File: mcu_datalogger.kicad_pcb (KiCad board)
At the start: 2 copper layers, 0 parts

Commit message: Prepared PCB
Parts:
- added BT1: Battery, Connector_PinHeader_2.54mm:PinHeader_1x01_P2.54mm_Vertical, F.Cu at (215.1, 142.3)
- added C1: 0.1uF, Capacitor_SMD:C_0805_2012Metric, F.Cu at (237.3, 132.0)
- added C2: 22pF, Capacitor_SMD:C_0805_2012Metric, F.Cu at (237.3, 135.1)
- added C3: 22pF, Capacitor_SMD:C_0805_2012Metric, F.Cu at (237.3, 138.1)
- added C4: 0.1uF, Capacitor_SMD:C_0805_2012Metric, F.Cu at (237.3, 141.1)
- added C5: 100nF, Capacitor_SMD:C_0805_2012Metric, F.Cu at (237.3, 144.1)
- added D1: LED, LED_SMD:LED_0805_2012Metric, F.Cu at (241.8, 132.1)
- added D2: LED, LED_SMD:LED_0805_2012Metric, F.Cu at (241.8, 135.1)
- added H1: MountingHole, MountingHole:MountingHole_2.1mm, F.Cu at (215.6, 119.9)
- added H2: MountingHole, MountingHole:MountingHole_2.1mm, F.Cu at (215.6, 125.6)
- added H3: MountingHole, MountingHole:MountingHole_2.1mm, F.Cu at (215.6, 131.4)
- added H4: MountingHole, MountingHole:MountingHole_2.1mm, F.Cu at (215.6, 137.1)
- added J1: Conn_01x04_Pin, Connector_PinHeader_2.54mm:PinHeader_1x04_P2.54mm_Vertical, F.Cu at (253.0, 119.3)
- added J2: Conn_01x04_Pin, Connector_PinHeader_2.54mm:PinHeader_1x04_P2.54mm_Vertical, F.Cu at (257.6, 119.3)
- added J3: Conn_02x03_Odd_Even, Connector_PinHeader_2.54mm:PinHeader_2x03_P2.54mm_Vertical, F.Cu at (253.0, 131.6)
- added J4: Conn_01x09_Pin, Connector_PinHeader_2.54mm:PinHeader_1x09_P2.54mm_Vertical, F.Cu at (248.3, 119.3)
- added R1: 10K, Resistor_SMD:R_0805_2012Metric, F.Cu at (220.7, 118.5)
- added R2: 10K, Resistor_SMD:R_0805_2012Metric, F.Cu at (220.7, 121.4)
- added R3: 4.7K, Resistor_SMD:R_0805_2012Metric, F.Cu at (220.7, 124.4)
- added R4: 4.7K, Resistor_SMD:R_0805_2012Metric, F.Cu at (220.7, 127.3)
- added R5: 330, Resistor_SMD:R_0805_2012Metric, F.Cu at (220.7, 130.3)
- added R6: 10K, Resistor_SMD:R_0805_2012Metric, F.Cu at (220.7, 133.2)
- added R7: 330, Resistor_SMD:R_0805_2012Metric, F.Cu at (220.7, 136.2)
- added U1: 24LC1025, Package_SO:SOIC-8_5.23x5.23mm_P1.27mm, F.Cu at (228.1, 120.4)
- added U2: 24LC1025, Package_SO:SOIC-8_5.23x5.23mm_P1.27mm, F.Cu at (228.1, 127.2)
- added U3: ATMEGA328P-AU, Footprints:QFP80P900X900X120-32N, F.Cu at (229.4, 136.2)
- added U4: DS1337S_, Footprints:SOIC127P600X175-8N, F.Cu at (228.0, 145.2)
- added Y1: 32.768 KHz, Crystal:Crystal_SMD_5032-2Pin_5.0x3.2mm_HandSoldering, F.Cu at (238.4, 119.4)
- added Y2: 16 MHz, Crystal:Crystal_SMD_5032-2Pin_5.0x3.2mm_HandSoldering, F.Cu at (238.4, 124.3)

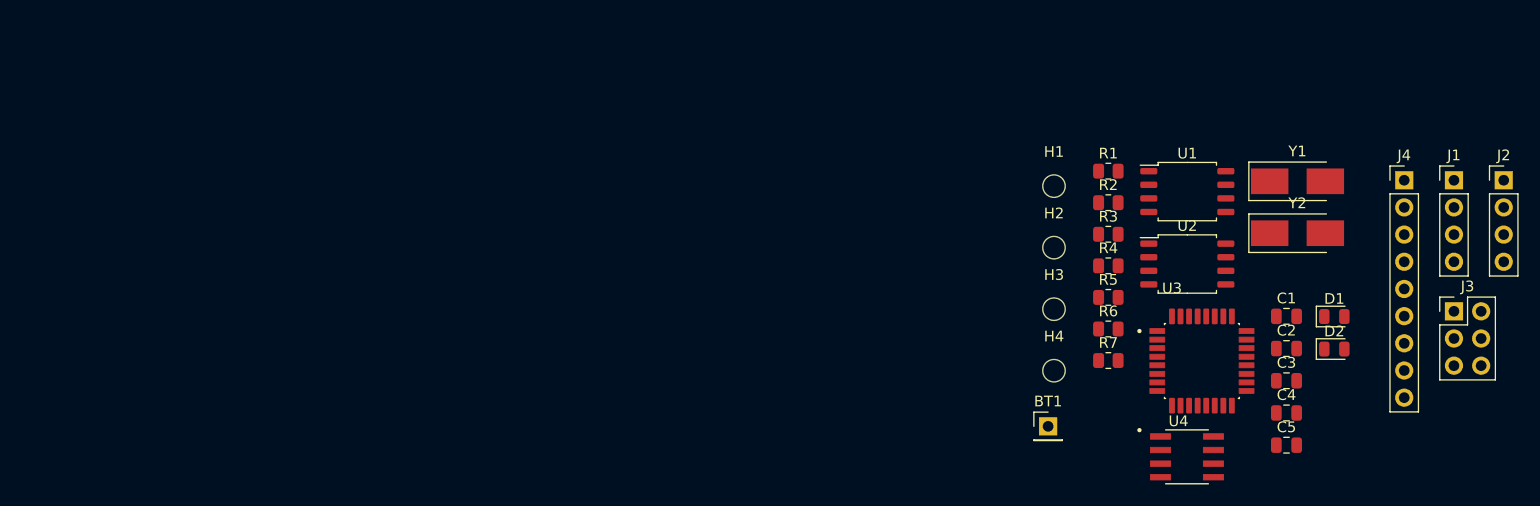
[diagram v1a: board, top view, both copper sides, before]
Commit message: Completed placement of footprints
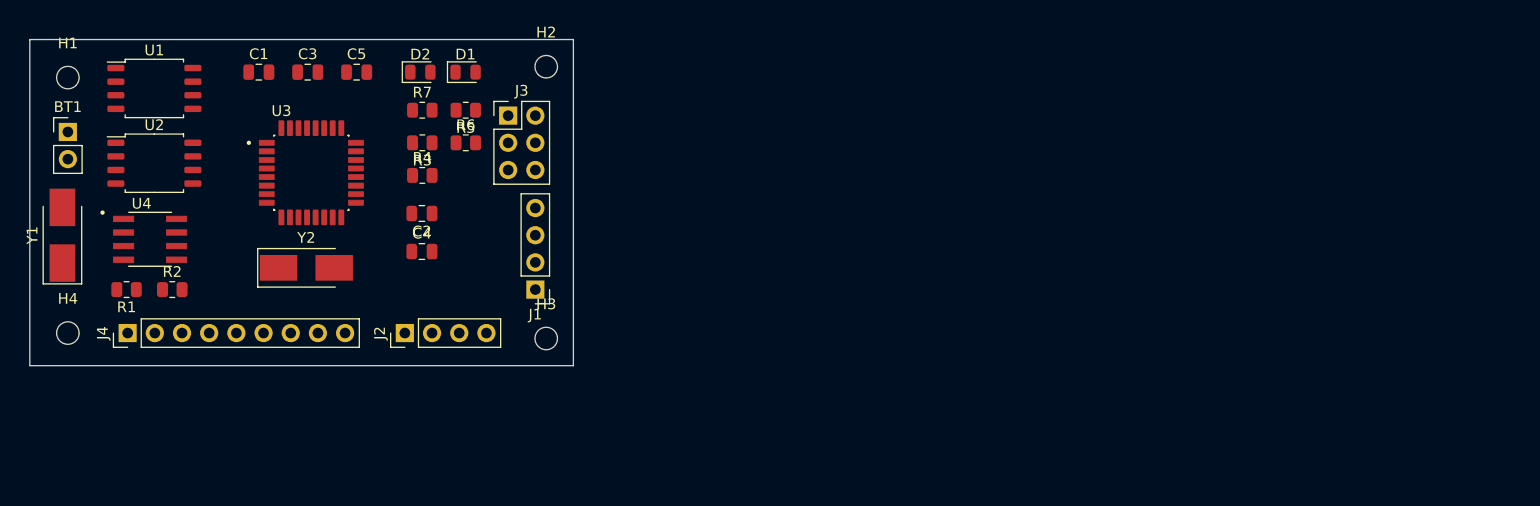
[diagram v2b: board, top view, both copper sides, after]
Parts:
- BT1: footprint Connector_PinHeader_2.54mm:PinHeader_1x01_P2.54mm_Vertical -> Connector_PinHeader_2.54mm:PinHeader_1x02_P2.54mm_Vertical
- moved J4 120.2 mm to (129.0, 133.6), turned to 90 degrees
- moved Y1 115.5 mm to (122.9, 124.5), turned to 90 degrees
- moved J2 103.7 mm to (154.9, 133.6), turned to 90 degrees
- moved U4 99.0 mm to (131.1, 124.8)
- moved C1 98.7 mm to (141.3, 109.2)
- moved U1 97.0 mm to (131.5, 110.7)
- moved U2 97.0 mm to (131.5, 117.7)
- moved C3 95.9 mm to (145.9, 109.2)
- moved BT1 95.7 mm to (123.4, 114.8)
- moved C5 93.6 mm to (150.4, 109.2)
- moved H1 92.7 mm to (123.4, 109.7)
- moved Y2 92.7 mm to (145.7, 127.5)
- moved R1 92.4 mm to (128.9, 129.5), turned to 180 degrees
- moved H4 92.2 mm to (123.4, 133.6)
- moved J3 90.3 mm to (164.6, 113.3)
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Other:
- board outline added: 50.8 x 30.5 mm

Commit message: Routing first version
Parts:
- moved J1 7.37 mm to (167.1, 122.2), turned to 0 degrees
- moved U1 6.99 mm to (131.6, 117.7)
- moved U2 6.99 mm to (131.6, 110.7)
- moved R3 3.30 mm to (156.6, 119.1)
- moved R4 3.05 mm to (156.6, 115.8)
- moved H1 1.26 mm to (122.6, 108.8)
- moved R1 0.71 mm to (129.6, 129.5), turned to 0 degrees
- moved R2 0.51 mm to (133.7, 129.5)
- moved U4 0.51 mm to (131.6, 124.8)
- moved C5 0.40 mm to (150.6, 108.8)
- moved C1 0.39 mm to (141.2, 108.8), turned to 180 degrees
- moved C3 0.38 mm to (145.9, 108.8)
- moved H3 0.18 mm to (168.3, 134.2)
- moved D2 0.16 mm to (156.5, 109.2)
- turned R7 to 180 degrees
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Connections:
- U3 pad 4: unconnected-(U3-VCC-Pad4) -> Net-(BT1-+)
- U3 pad 6: Net-(BT1-+) -> unconnected-(U3-VCC-Pad6)
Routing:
- net /SCK: track 0.00 -> 94.1 mm, vias 0 -> 4
- net VCC: track 0.00 -> 87.7 mm, vias 0 -> 1
- net Net-(BT1-+): track 0.00 -> 65.1 mm, vias 0 -> 5
- net /SDA: track 0.00 -> 58.7 mm, vias 0 -> 2
- net GND: track 0.00 -> 54.4 mm, vias 0 -> 6
- net Net-(U3-PB7): track 0.00 -> 32.0 mm, vias 0 -> 2
- net /RX: track 0.00 -> 28.3 mm, vias 0 -> 1
- net Net-(U3-PB6): track 0.00 -> 27.7 mm
- net /TX: track 0.00 -> 27.3 mm, vias 0 -> 1
- net /D2: track 0.00 -> 27.1 mm, vias 0 -> 1
- net /MOSI: track 0.00 -> 24.1 mm
- net /RESET: track 0.00 -> 23.3 mm, vias 0 -> 4
- net /D3: track 0.00 -> 22.8 mm
- net /MISO: track 0.00 -> 21.2 mm, vias 0 -> 1
- net /D4: track 0.00 -> 20.6 mm
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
